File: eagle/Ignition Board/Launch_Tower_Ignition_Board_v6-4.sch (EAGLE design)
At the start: 41 parts, among them IC1 INVERT GATES, IC2 OPTOISOLATOR, Q1 NMOSFET, U1 SN65220DBV

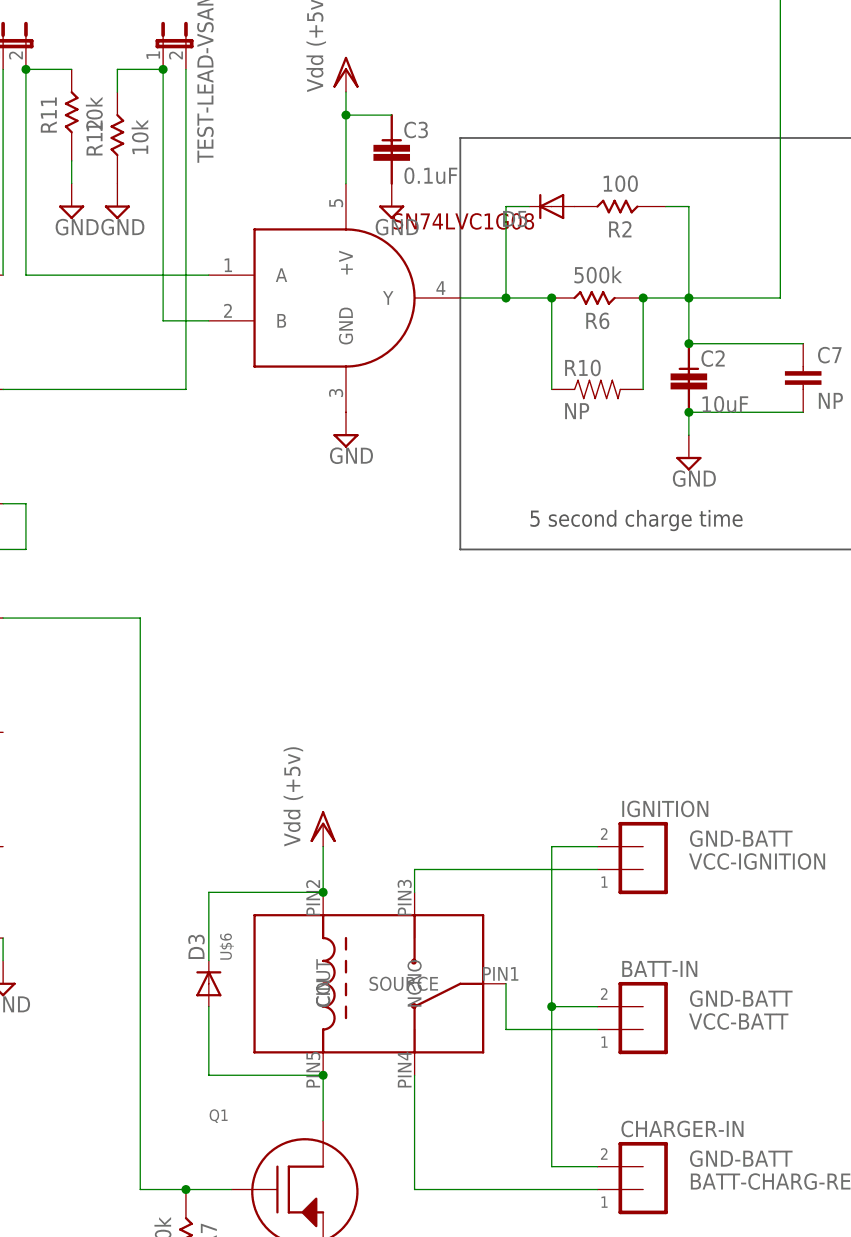
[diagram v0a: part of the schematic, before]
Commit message: Minor changes to Ignition board and library - smaller diode Signed-off-by: richard <richard@mailwh.com>
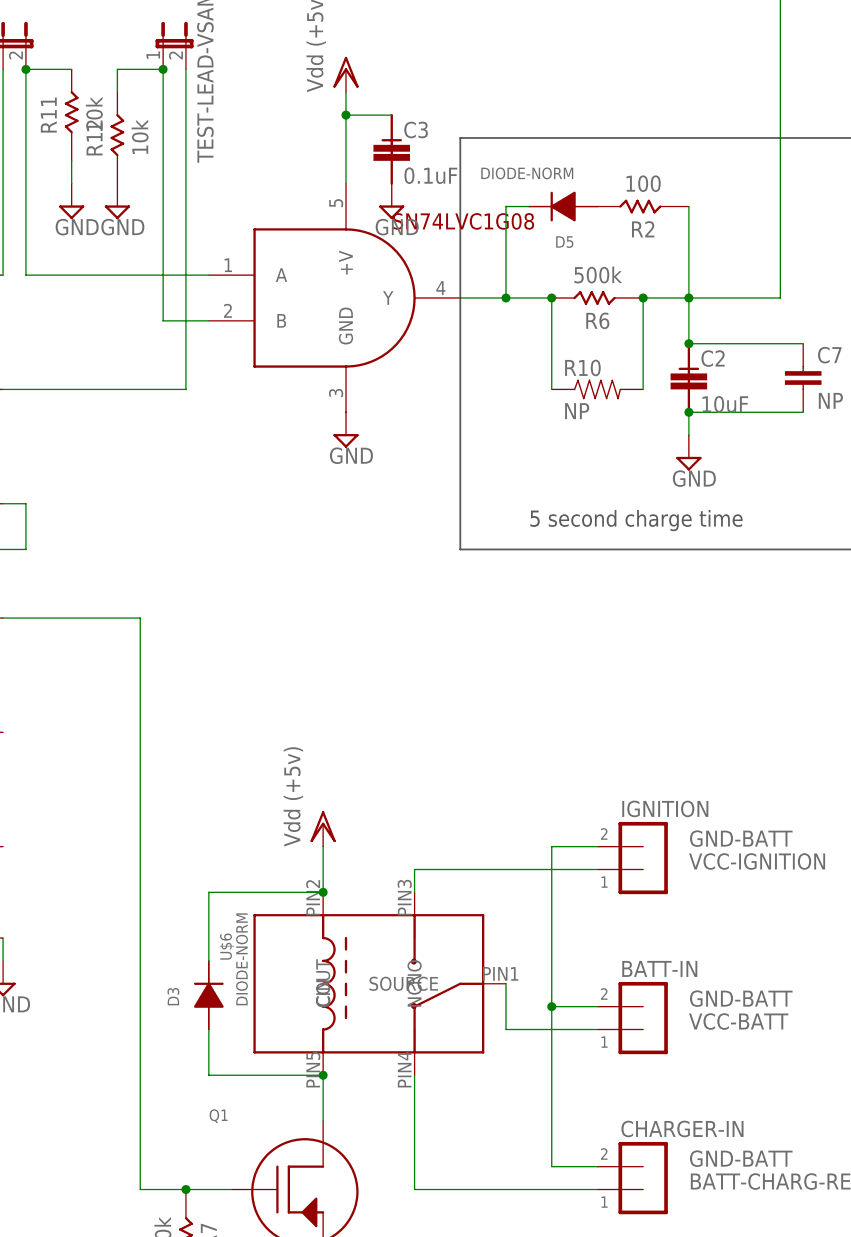
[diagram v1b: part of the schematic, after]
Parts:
- D3, D5: value (none) -> DIODE-NORM; device SparkFun:DIODEPTH -> launch-tower:DIODE-NORM
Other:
- moved on the sheet: D3, D5, R2
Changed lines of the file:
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@@
 <part name="JP2" library="launch-tower" deviceset="SCREW-TERMINAL-5MM" device="" value=""/>
 <part name="JP3" library="launch-tower" deviceset="SCREW-TERMINAL-5MM" device="" value=""/>
-<part name="D5" library="SparkFun" deviceset="DIODE" device="PTH"/>
-<part name="D3" library="SparkFun" deviceset="DIODE" device="PTH"/>
+<part name="D5" library="launch-tower" deviceset="DIODE-NORM" device=""/>
+<part name="D3" library="launch-tower" deviceset="DIODE-NORM" device=""/>
 <part name="VDD2" library="supply1" deviceset="VDD" device="" value="Vdd (+5v)"/>
 <part name="SUPPLY13" library="supply2" deviceset="GND" device=""/>
@@
 <instance part="R9" gate="R$1" x="35.56" y="187.96" rot="R90"/>
 <instance part="SUPPLY19" gate="GND" x="177.8" y="177.8"/>
-<instance part="R2" gate="R$1" x="238.76" y="177.8" rot="R180"/>
+<instance part="R2" gate="R$1" x="241.3" y="177.8" rot="R180"/>
 <instance part="C4" gate="G$1" x="129.54" y="185.42"/>
 <instance part="C5" gate="G$1" x="35.56" y="177.8"/>
@@
 <junction x="241.3" y="167.64"/>
 <pinref part="R2" gate="R$1" pin="ANODE"/>
-<wire x1="246.38" y1="177.8" x2="243.84" y2="177.8" width="0.1524" layer="91"/>
 <pinref part="C2" gate="G$1" pin="ANODE"/>
 <junction x="246.38" y="162.56"/>
@@
 <wire x1="205.74" y1="81.28" x2="205.74" y2="76.2" width="0.1524" layer="91"/>
 <wire x1="205.74" y1="81.28" x2="193.04" y2="81.28" width="0.1524" layer="91"/>
-<wire x1="193.04" y1="81.28" x2="193.04" y2="88.9" width="0.1524" layer="91"/>
+<wire x1="193.04" y1="81.28" x2="193.04" y2="86.36" width="0.1524" layer="91"/>
 <pinref part="D3" gate="G$1" pin="A"/>
 <pinref part="U$6" gate="G$1" pin="CIN"/>

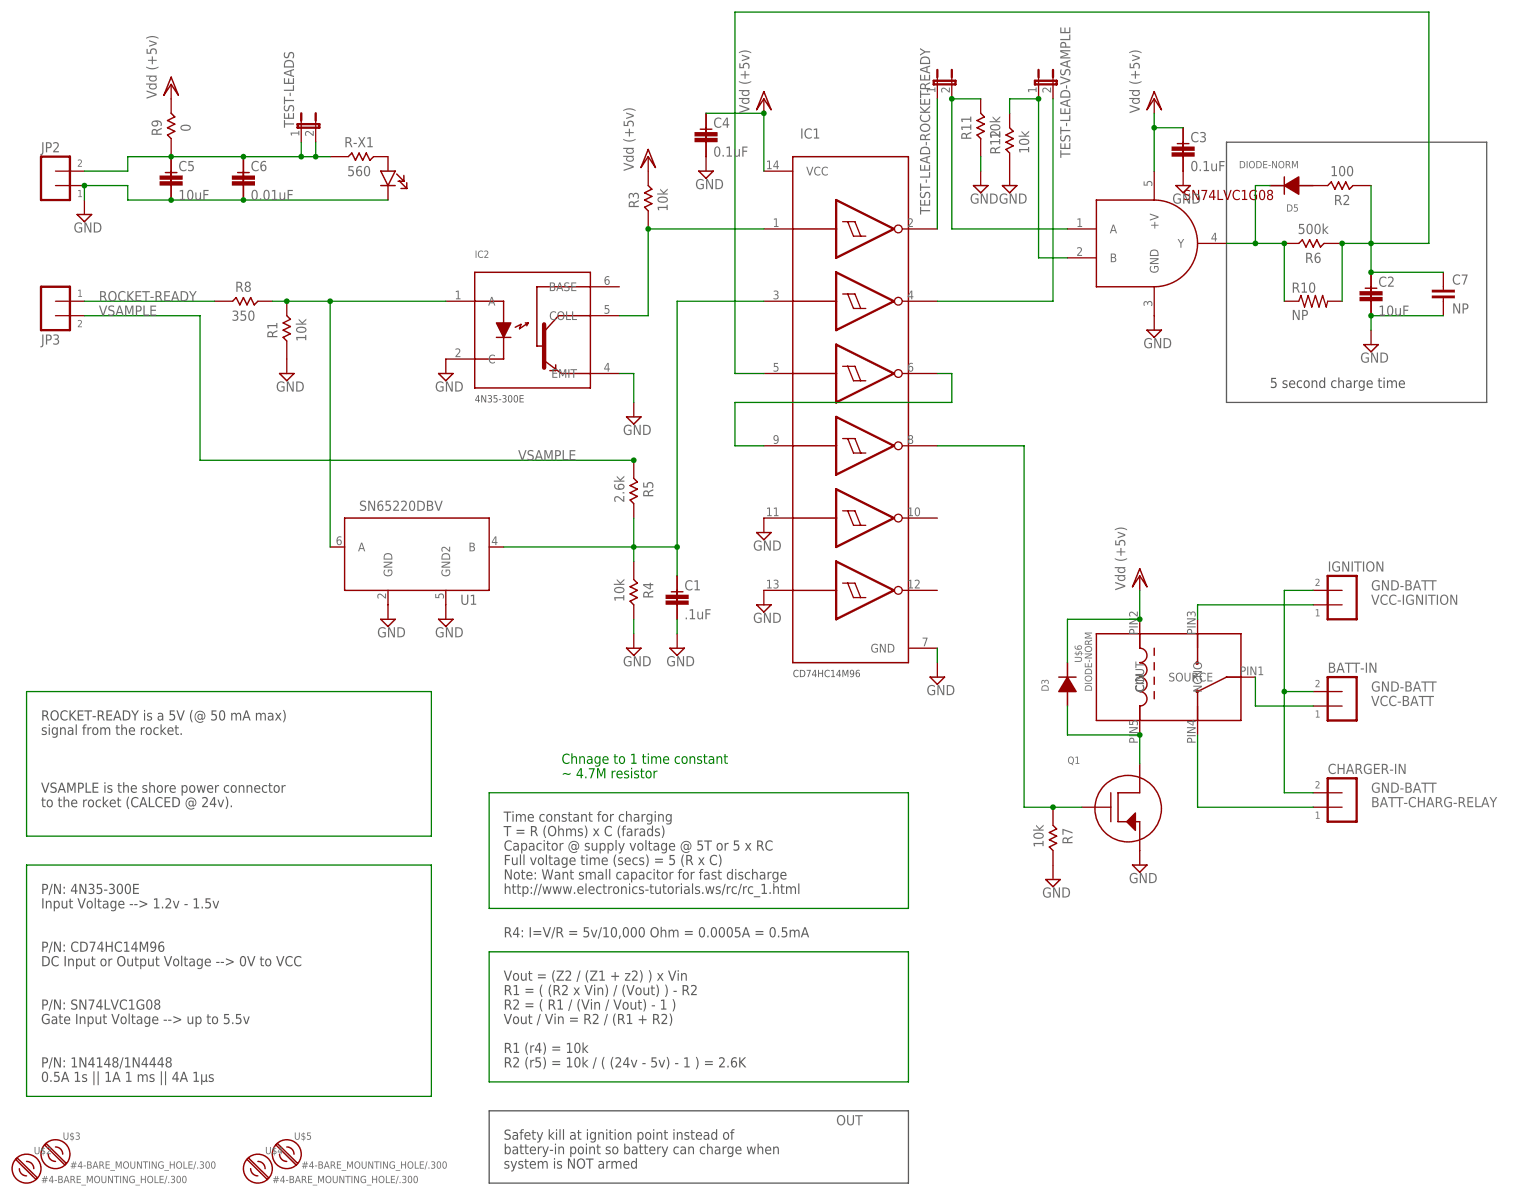
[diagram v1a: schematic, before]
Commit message: Cleaned up ignition board for manufacturing - ERCs, DRCs, flood fills, switched MOSFET to have a higher Vgs on, added LED for the ignition on circuit, cleaned up tsilk layer.
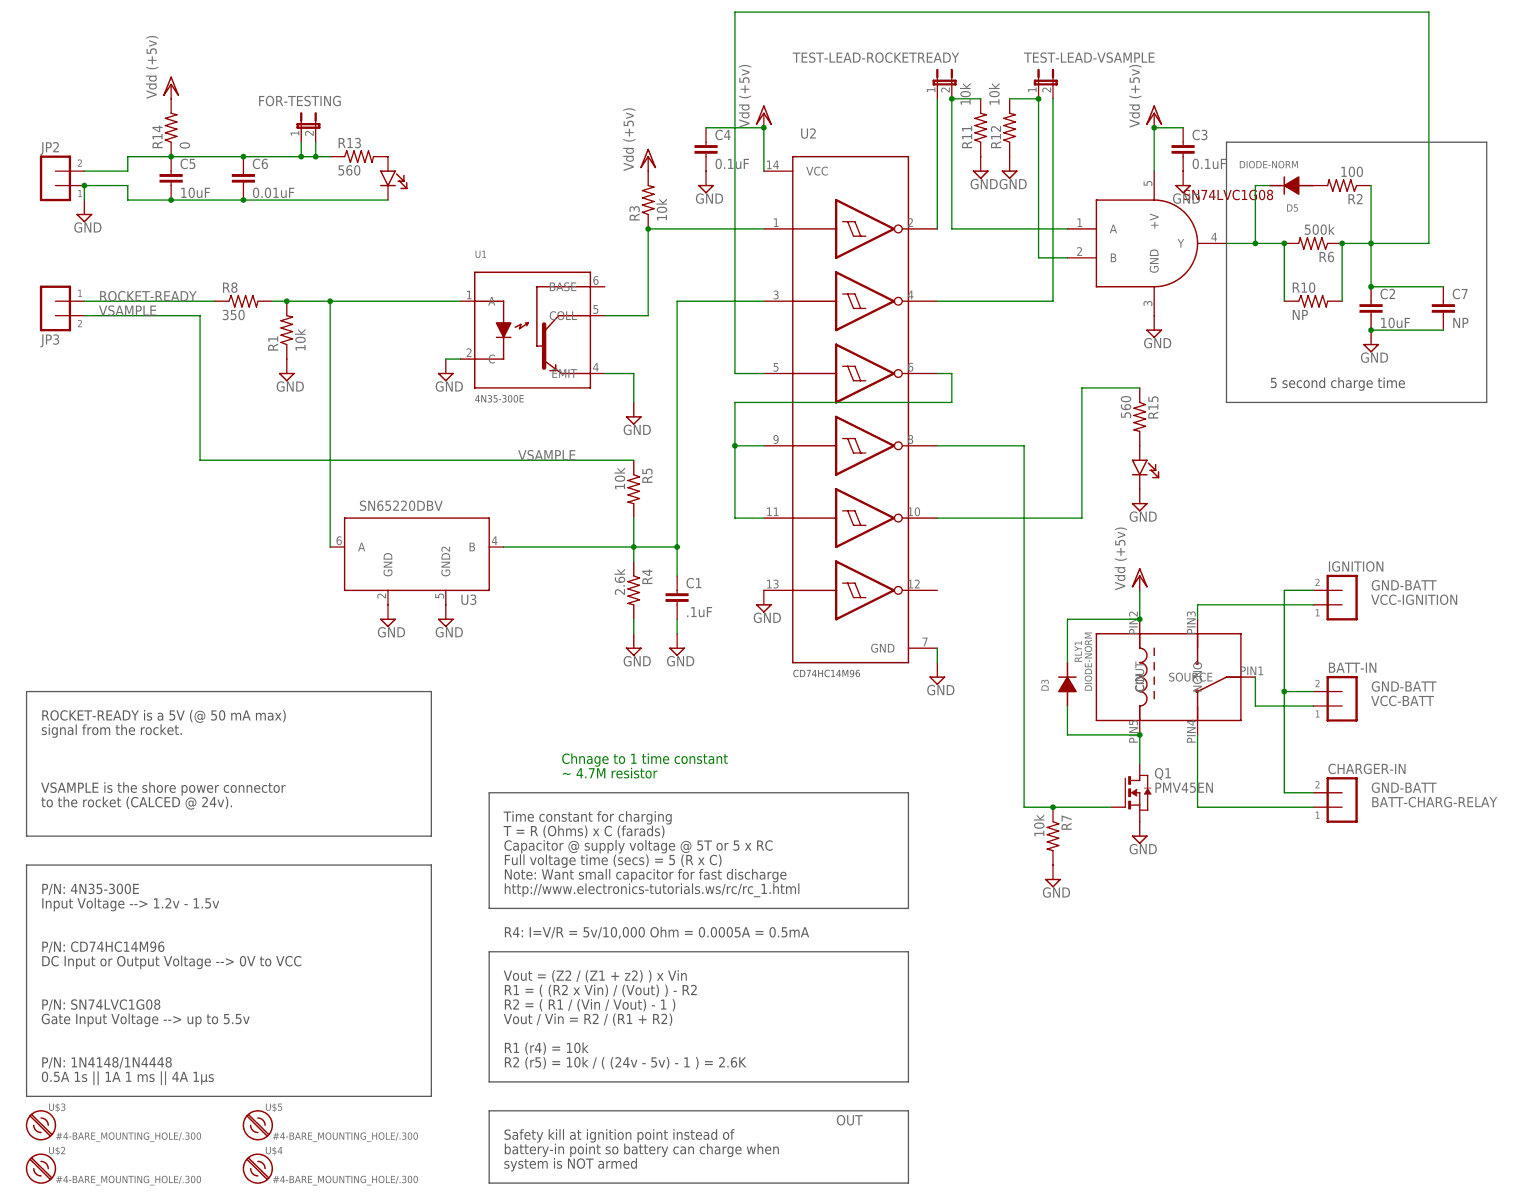
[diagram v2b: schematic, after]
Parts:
- removed IC2: OPTOISOLATOR, launch-tower:OPTOISOLATOR
- removed R-X1: 560, launch-tower:RESISTOR-0805
- removed R9: 0, launch-tower:RESISTOR-0805
- added LED-POWER-INDICATOR1: LED-550-XX04, launch-tower:LED-550-XX04
- added R13, R15: 560, rcl_custom:R-US_0805-B
- added R14: 0, rcl_custom:R-US_0805-B
- added U3: SN65220DBV, sn65220:SN65220DBV
- C1, C2, C3, C4, C5, C6: device launch-tower:CAPACITOR-0805 -> rcl_custom:C-EU0805-B
- Q1: value NMOSFET -> PMV45EN; device launch-tower:NMOSFET -> Tova:PMV45EN
- R1, R11, R12, R2, R3, R6, R7, R8: device launch-tower:RESISTOR-0805 -> rcl_custom:R-US_0805-B
- R10: device SparkFun:RESISTORPTH-1/4W -> rcl_custom:R-US_0207/10
- R4: value 10k -> 2.6k; device launch-tower:RESISTOR-0805 -> rcl_custom:R-US_0805-B
- R5: value 2.6k -> 10k; device launch-tower:RESISTOR-0805 -> rcl_custom:R-US_0805-B
- U1: value SN65220DBV -> OPTOISOLATOR; device sn65220:SN65220DBV -> launch-tower:OPTOISOLATOR
- renumbered IC1 to U2, TEST-LEADS to FOR-TESTING, U$1 to U4, U$6 to RLY1
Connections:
- removed net GND: C1.CATHODE, C2.CATHODE, C3.CATHODE, C4.CATHODE, C5.CATHODE, C6.CATHODE, C7.2, IC2.C, IC2.EMIT, JP2.1, LED-POWER-INDICATOR.CATHODE, Q1.SOURCE, R1.ANODE, R11.ANODE, R12.ANODE, R4.CATHODE, R7.CATHODE, U1.GND, U1.GND2, U2.5A, U2.6A, U2.GND, U4.GND
- new net N$14: R15.1, U2.5Y
- new net N$18: LED-POWER-INDICATOR1.ANODE, R15.2
- new net NAME: C1.2, C2.2, C3.2, C4.2, C5.2, C6.2, C7.2, JP2.1, LED-POWER-INDICATOR.CATHODE, LED-POWER-INDICATOR1.CATHODE, Q1.S, R1.1, R11.1, R12.1, R4.2, R7.2, U1.C, U1.EMIT, U2.6A, U2.GND, U3.GND, U3.GND2, U4.GND
- net N$1: now also R12.2; no longer R12.CATHODE
- net N$10: now also Q1.G, R7.1; no longer Q1.GATE, R7.ANODE
- net N$12: now also C5.1, C6.1, R13.1, R14.1; no longer C5.ANODE, C6.ANODE, R-X1.ANODE, R9.ANODE
- net N$13: now also R6.2; no longer R6.CATHODE
- net N$15: now also C2.1, R2.1, R6.1; no longer C2.ANODE, R2.ANODE, R6.ANODE
- net N$2: now also R13.2; no longer R-X1.CATHODE
- net N$3: now also R3.1, U1.COLL; no longer IC2.COLL, R3.ANODE
- net N$4: now also R8.1; no longer R8.ANODE
- net N$5: now also R11.2; no longer R11.CATHODE
- net N$7: now also C1.1, R4.1, R5.2, U3.B; no longer C1.ANODE, R4.ANODE, R5.CATHODE, U1.B
- net N$8: now also R2.2; no longer R2.CATHODE
- net N$9: now also Q1.D; no longer Q1.DRAIN
- net N-NOT2: now also U2.5A
- net ROCKET-READY: now also R1.2, R8.2, U3.A; no longer IC2.A, R1.CATHODE, R8.CATHODE
- net VDD: now also C3.1, C4.1, R14.2, R3.2; no longer C3.ANODE, C4.ANODE, R3.CATHODE, R9.CATHODE
- net VSAMPLE: now also R5.1; no longer R5.ANODE
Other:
- moved on the sheet: C7, U$2, U$3, U$5
